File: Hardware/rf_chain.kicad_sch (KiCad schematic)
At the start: 10 parts, among them J1 132225, J3 132225, U1 Si4464, U2 Si4464

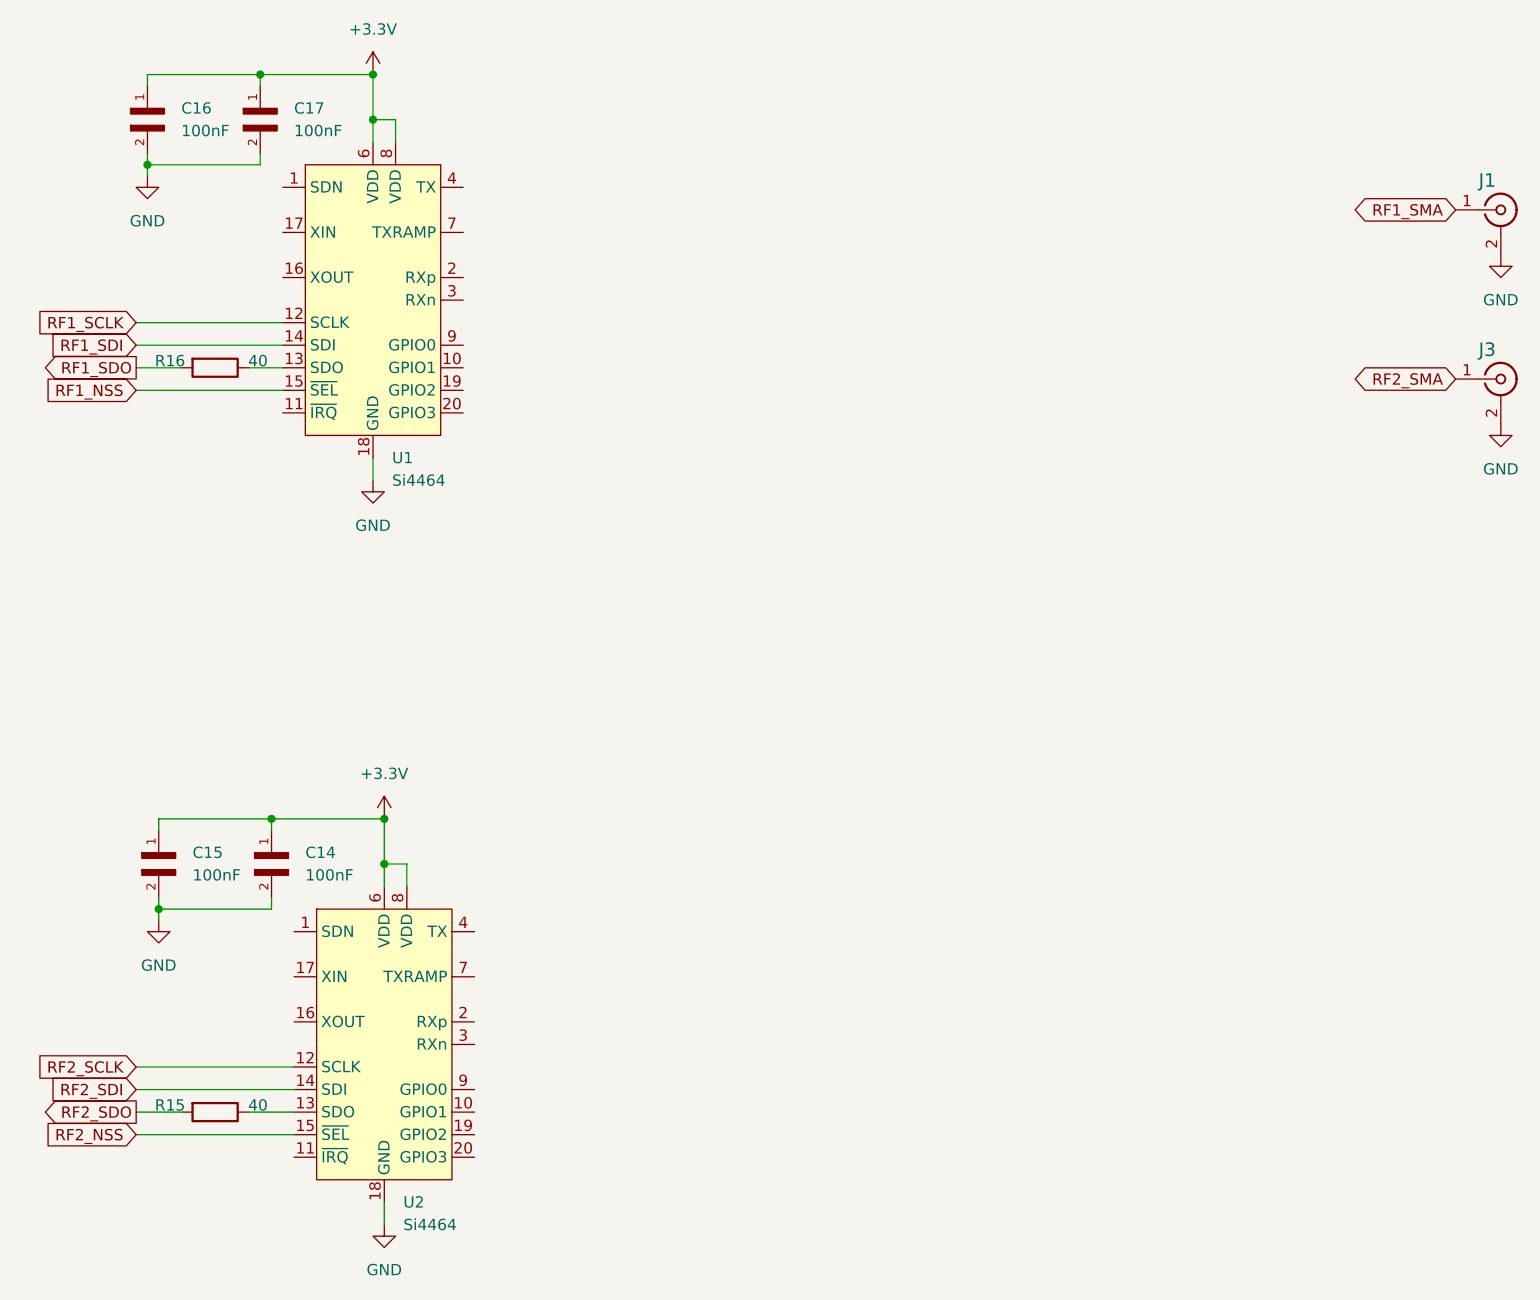
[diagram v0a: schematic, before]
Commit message: shutdown pin connection to RF chain
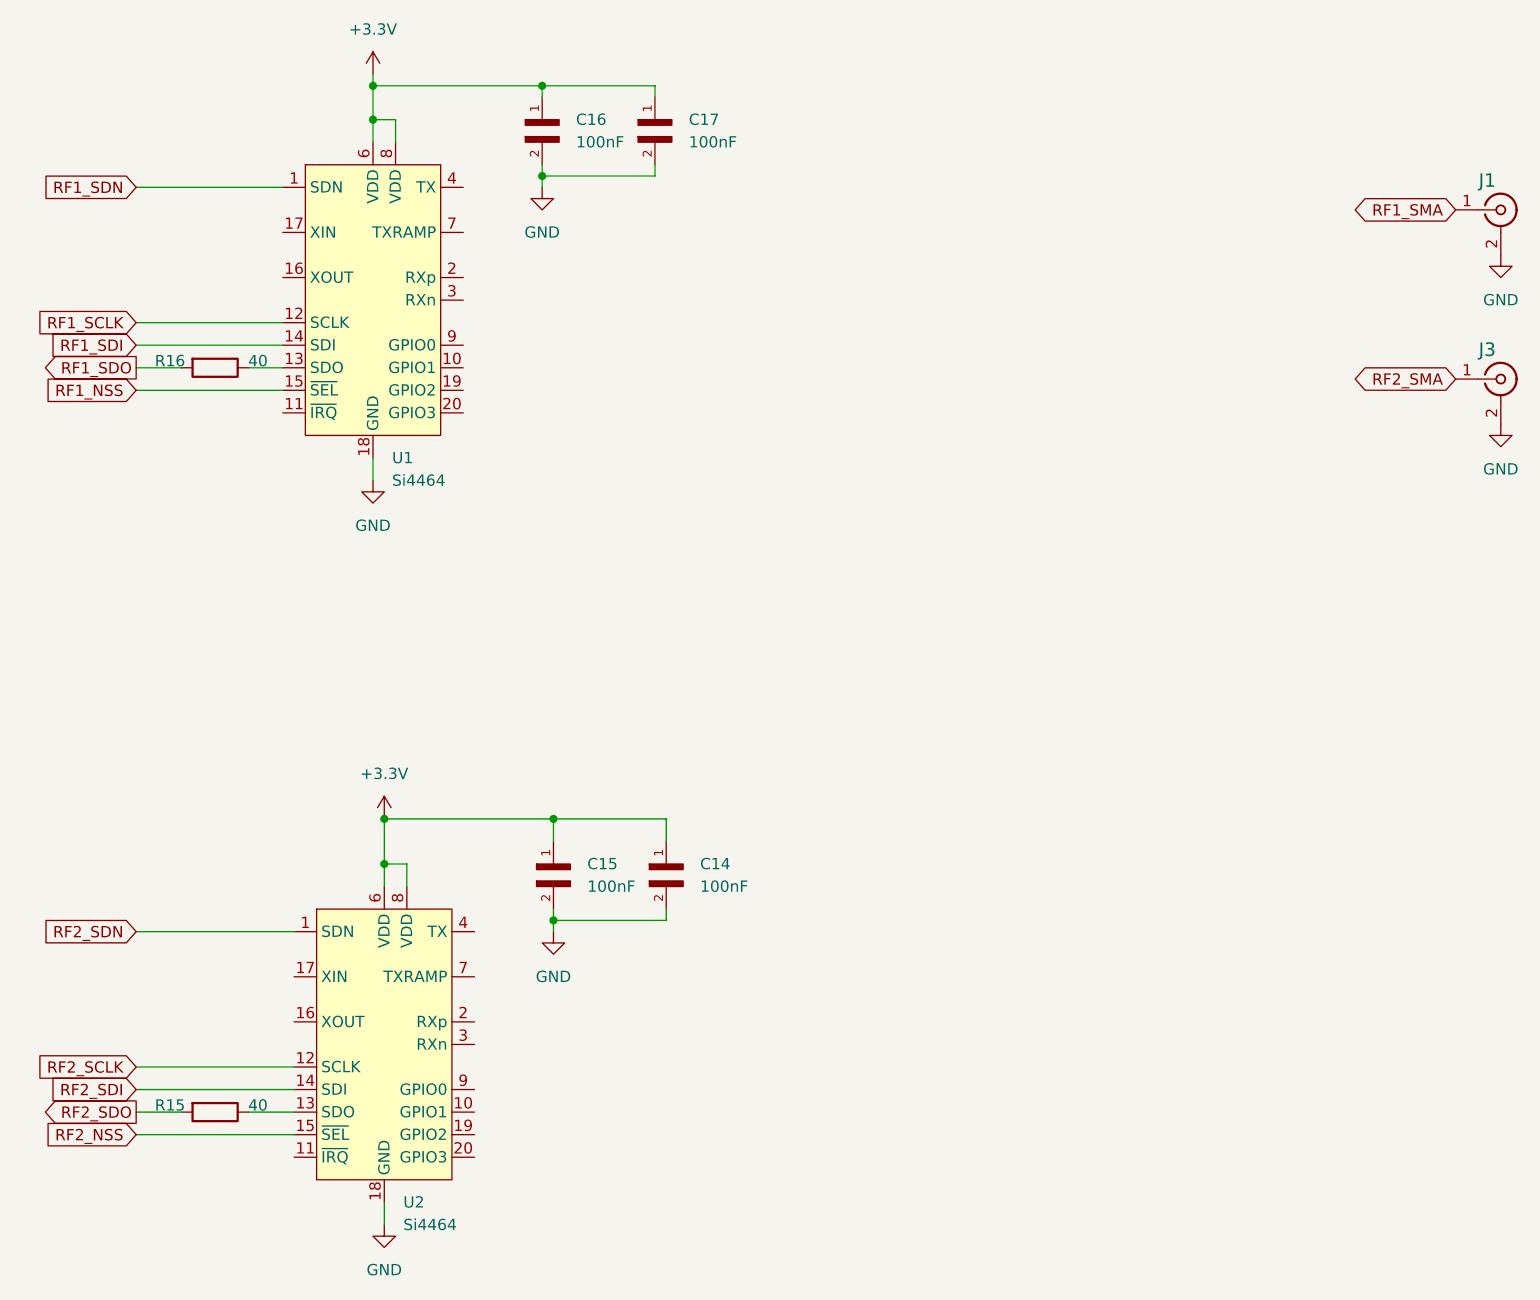
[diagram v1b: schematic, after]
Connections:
- net RF1_SDN: now reaches U1.1 (SDN)
- net RF2_SDN: now reaches U2.1 (SDN)
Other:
- moved on the sheet: C14, C15, C16, C17

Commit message: Finished Ethernet connection between MAC and PHY
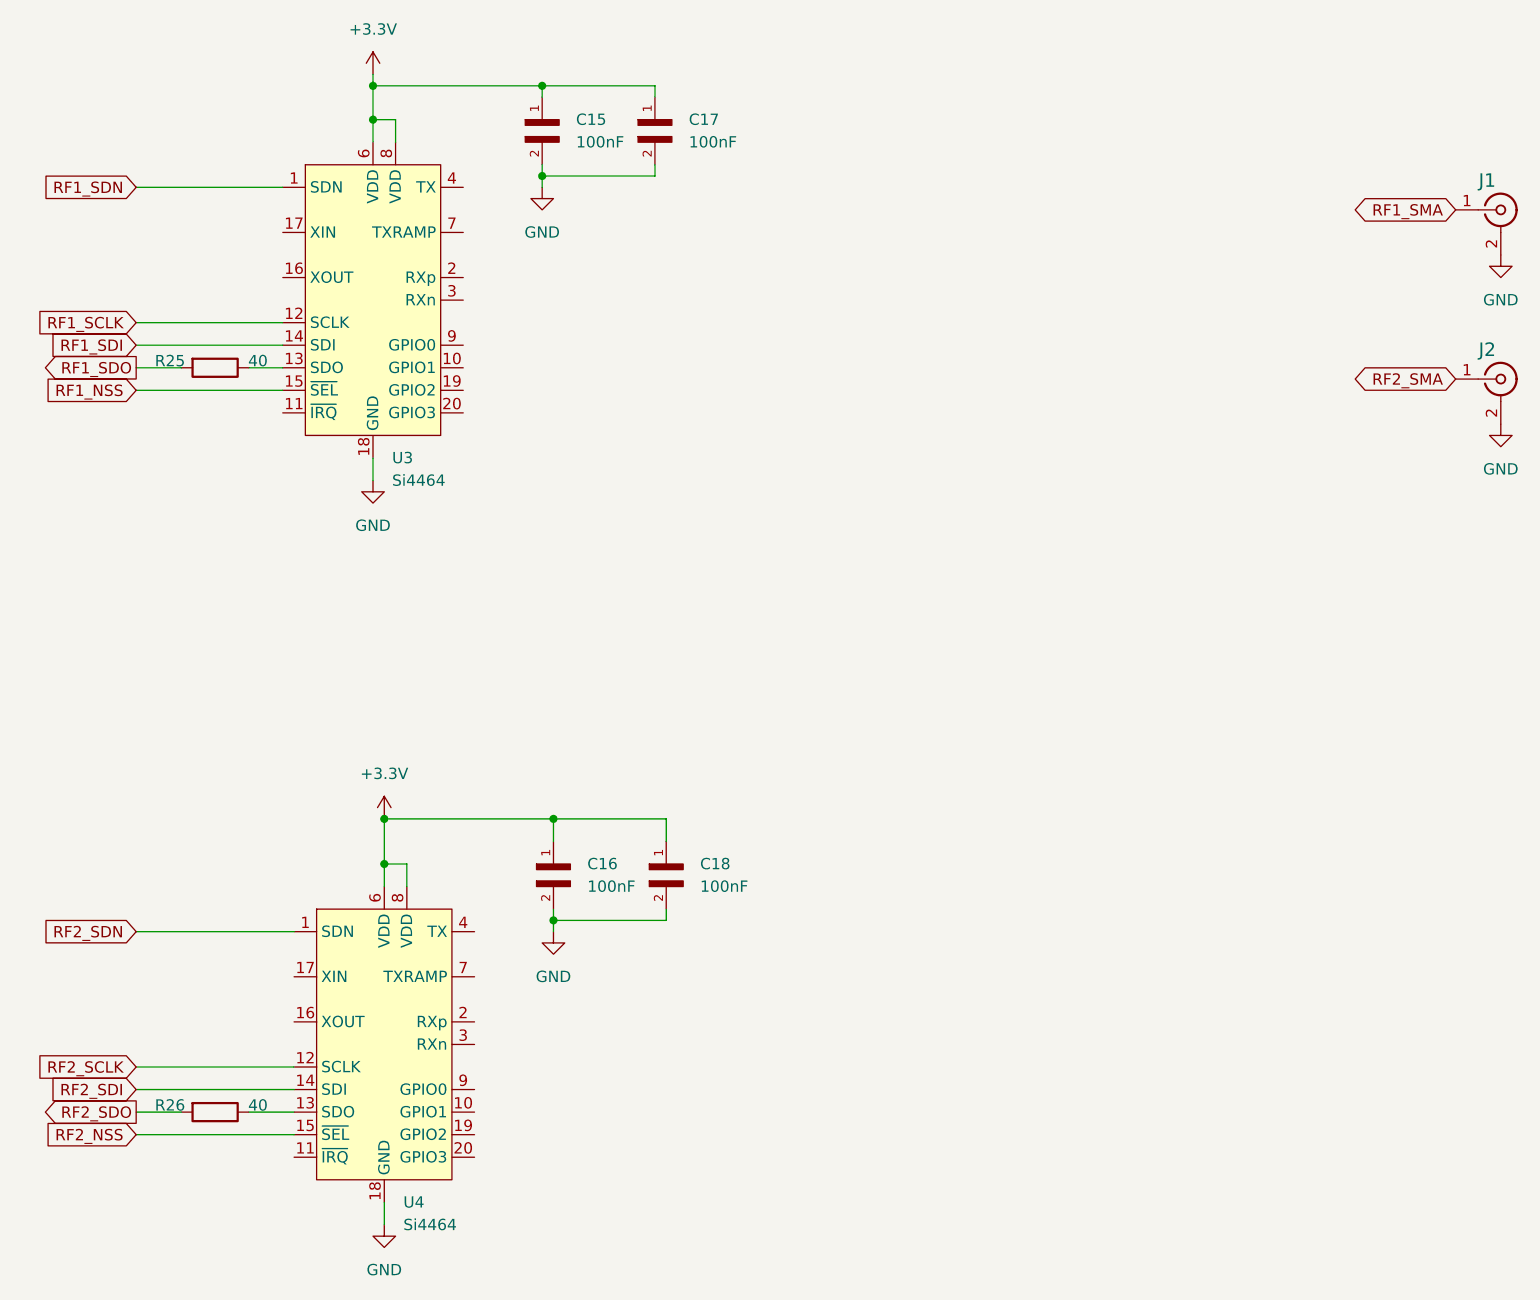
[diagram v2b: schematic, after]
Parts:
- renumbered C16 to C15, C15 to C16, C14 to C18, J3 to J2, R16 to R25, R15 to R26, U1 to U3, U2 to U4
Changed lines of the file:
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@@
 		(dnp no)
 		(fields_autoplaced yes)
-		(property "Reference" "#PWR029"
+		(property "Reference" "#PWR027"
 			(at 88.9 147.32 0)
 			(effects
@@
 			(project "Radio Project"
 				(path "/ca6389fe-9846-40e3-87a4-456cfcfc0777/2dc9614d-695e-43f1-a091-76db997bc2c6"
-					(reference "#PWR029")
+					(reference "#PWR027")
 					(unit 1)
 				)
@@
 		(dnp no)
 		(fields_autoplaced yes)
-		(property "Reference" "C14"
+		(property "Reference" "C18"
 			(at 105.41 133.3499 90)
 			(effects
@@
 			(project "Radio Project"
 				(path "/ca6389fe-9846-40e3-87a4-456cfcfc0777/2dc9614d-695e-43f1-a091-76db997bc2c6"
-					(reference "C14")
+					(reference "C18")
 					(unit 1)
 				)
@@
 		(dnp no)
 		(fields_autoplaced yes)
-		(property "Reference" "#PWR030"
+		(property "Reference" "#PWR026"
 			(at 87.63 63.5 0)
 			(effects
@@
 			(project "Radio Project"
 				(path "/ca6389fe-9846-40e3-87a4-456cfcfc0777/2dc9614d-695e-43f1-a091-76db997bc2c6"
-					(reference "#PWR030")
+					(reference "#PWR026")
 					(unit 1)
 				)
@@
 		(dnp no)
 		(fields_autoplaced yes)
-		(property "Reference" "C15"
+		(property "Reference" "C16"
 			(at 92.71 133.3499 90)
 			(effects
@@
 			(project "Radio Project"
 				(path "/ca6389fe-9846-40e3-87a4-456cfcfc0777/2dc9614d-695e-43f1-a091-76db997bc2c6"
-					(reference "C15")
+					(reference "C16")
 					(unit 1)
 				)
@@
 		(on_board yes)
 		(dnp no)
-		(property "Reference" "#PWR05"
+		(property "Reference" "#PWR025"
 			(at 69.85 180.34 0)
 			(effects
@@
 			(project "Radio Project"
 				(path "/ca6389fe-9846-40e3-87a4-456cfcfc0777/2dc9614d-695e-43f1-a091-76db997bc2c6"
-					(reference "#PWR05")
+					(reference "#PWR025")
 					(unit 1)
 				)
@@
 		(on_board yes)
 		(dnp no)
-		(property "Reference" "R16"
+		(property "Reference" "R25"
 			(at 45.72 76.708 90)
 			(effects
@@
 			(project "Radio Project"
 				(path "/ca6389fe-9846-40e3-87a4-456cfcfc0777/2dc9614d-695e-43f1-a091-76db997bc2c6"
-					(reference "R16")
+					(reference "R25")
 					(unit 1)
 				)
@@
 		(dnp no)
 		(fields_autoplaced yes)
-		(property "Reference" "U1"
+		(property "Reference" "U3"
 			(at 70.7233 87.63 0)
 			(effects
@@
 			(project "Radio Project"
 				(path "/ca6389fe-9846-40e3-87a4-456cfcfc0777/2dc9614d-695e-43f1-a091-76db997bc2c6"
-					(reference "U1")
+					(reference "U3")
 					(unit 1)
 				)
@@
 		(dnp no)
 		(fields_autoplaced yes)
-		(property "Reference" "#PWR01"
+		(property "Reference" "#PWR022"
 			(at 68.58 48.26 0)
 			(effects
@@
 			(project "Radio Project"
 				(path "/ca6389fe-9846-40e3-87a4-456cfcfc0777/2dc9614d-695e-43f1-a091-76db997bc2c6"
-					(reference "#PWR01")
+					(reference "#PWR022")
 					(unit 1)
 				)
@@
 		(dnp no)
 		(fields_autoplaced yes)
-		(property "Reference" "J3"
+		(property "Reference" "J2"
 			(at 194.056 75.438 0)
 			(effects
@@
 			(project ""
 				(path "/ca6389fe-9846-40e3-87a4-456cfcfc0777/2dc9614d-695e-43f1-a091-76db997bc2c6"
-					(reference "J3")
+					(reference "J2")
 					(unit 1)
 				)
@@
 		(dnp no)
 		(fields_autoplaced yes)
-		(property "Reference" "U2"
+		(property "Reference" "U4"
 			(at 71.9933 171.45 0)
 			(effects
@@
 			(project "Radio Project"
 				(path "/ca6389fe-9846-40e3-87a4-456cfcfc0777/2dc9614d-695e-43f1-a091-76db997bc2c6"
-					(reference "U2")
+					(reference "U4")
 					(unit 1)
 				)
@@
 		(dnp no)
 		(fields_autoplaced yes)
-		(property "Reference" "#PWR06"
+		(property "Reference" "#PWR023"
 			(at 68.58 96.52 0)
 			(effects
@@
 			(project "Radio Project"
 				(path "/ca6389fe-9846-40e3-87a4-456cfcfc0777/2dc9614d-695e-43f1-a091-76db997bc2c6"
-					(reference "#PWR06")
+					(reference "#PWR023")
 					(unit 1)
 				)
@@
 		(dnp no)
 		(fields_autoplaced yes)
-		(property "Reference" "#PWR032"
+		(property "Reference" "#PWR029"
 			(at 195.58 90.17 0)
 			(effects
@@
 			(project "Radio Project"
 				(path "/ca6389fe-9846-40e3-87a4-456cfcfc0777/2dc9614d-695e-43f1-a091-76db997bc2c6"
-					(reference "#PWR032")
+					(reference "#PWR029")
 					(unit 1)
 				)
@@
 		(dnp no)
 		(fields_autoplaced yes)
-		(property "Reference" "C16"
+		(property "Reference" "C15"
 			(at 91.44 49.5299 90)
 			(effects
@@
 			(project "Radio Project"
 				(path "/ca6389fe-9846-40e3-87a4-456cfcfc0777/2dc9614d-695e-43f1-a091-76db997bc2c6"
-					(reference "C16")
+					(reference "C15")
 					(unit 1)
 				)
@@
 		(dnp no)
 		(fields_autoplaced yes)
-		(property "Reference" "#PWR031"
+		(property "Reference" "#PWR028"
 			(at 195.58 71.12 0)
 			(effects
@@
 			(project "Radio Project"
 				(path "/ca6389fe-9846-40e3-87a4-456cfcfc0777/2dc9614d-695e-43f1-a091-76db997bc2c6"
-					(reference "#PWR031")
+					(reference "#PWR028")
 					(unit 1)
 				)
@@
 		(on_board yes)
 		(dnp no)
-		(property "Reference" "R15"
+		(property "Reference" "R26"
 			(at 45.72 160.528 90)
 			(effects
@@
 			(project "Radio Project"
 				(path "/ca6389fe-9846-40e3-87a4-456cfcfc0777/2dc9614d-695e-43f1-a091-76db997bc2c6"
-					(reference "R15")
+					(reference "R26")
 					(unit 1)
 				)
@@
 		(dnp no)
 		(fields_autoplaced yes)
-		(property "Reference" "#PWR02"
+		(property "Reference" "#PWR024"
 			(at 69.85 132.08 0)
 			(effects
@@
 			(project "Radio Project"
 				(path "/ca6389fe-9846-40e3-87a4-456cfcfc0777/2dc9614d-695e-43f1-a091-76db997bc2c6"
-					(reference "#PWR02")
-					(unit 1)
-				)
+					(reference "#PWR024")
+					(unit 1)
+				)
